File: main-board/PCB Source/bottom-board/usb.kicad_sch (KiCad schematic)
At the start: 17 parts, among them P1 USB_B, P2 USB_A, U10 TPS2001DDBVR

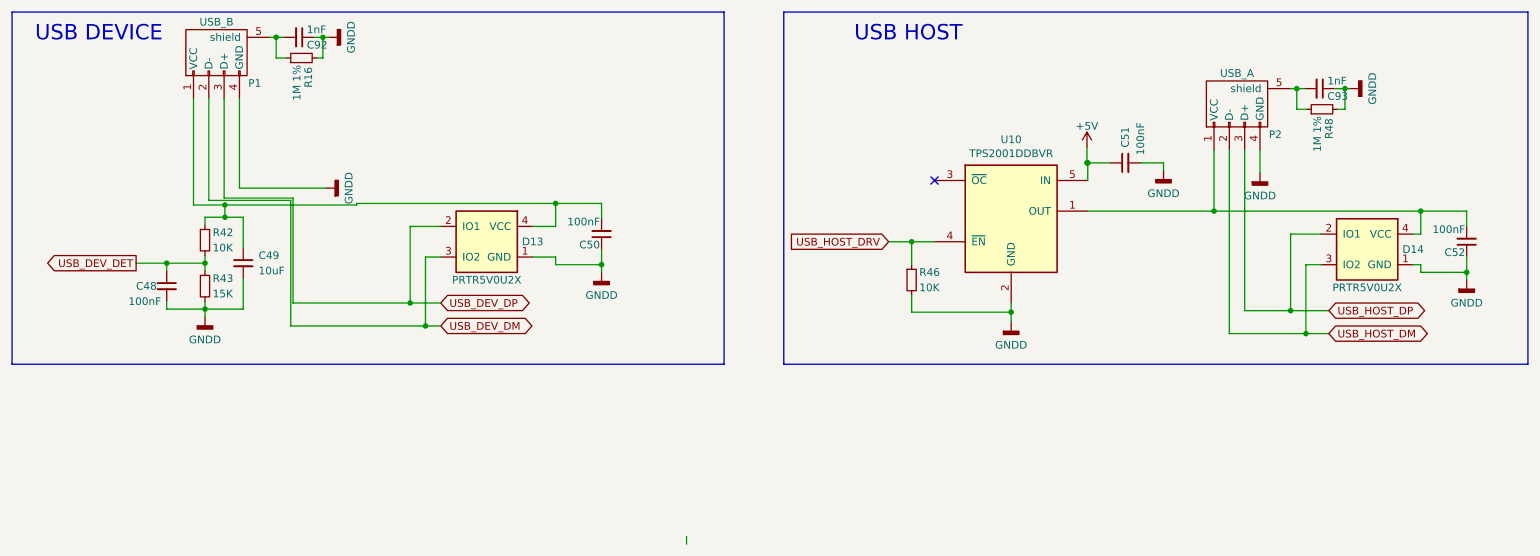
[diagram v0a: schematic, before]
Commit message: mainboard: add bias buffer, update MPNs, clean schematic
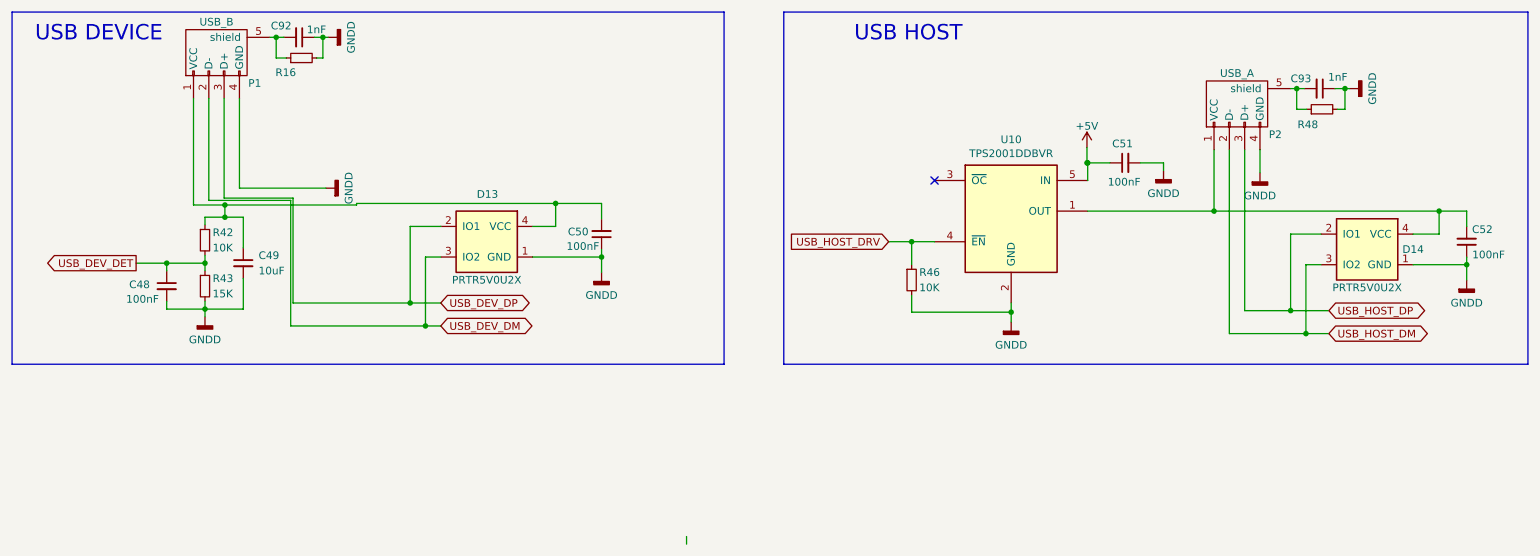
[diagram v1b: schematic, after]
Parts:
- C92, C93: MPN C0603X7R500-103KNP -> C0603X7R500-102KNP
- R16, R48: value 1M 1% -> (none); footprint Resistor_SMD:R_0603_1608Metric -> (none)

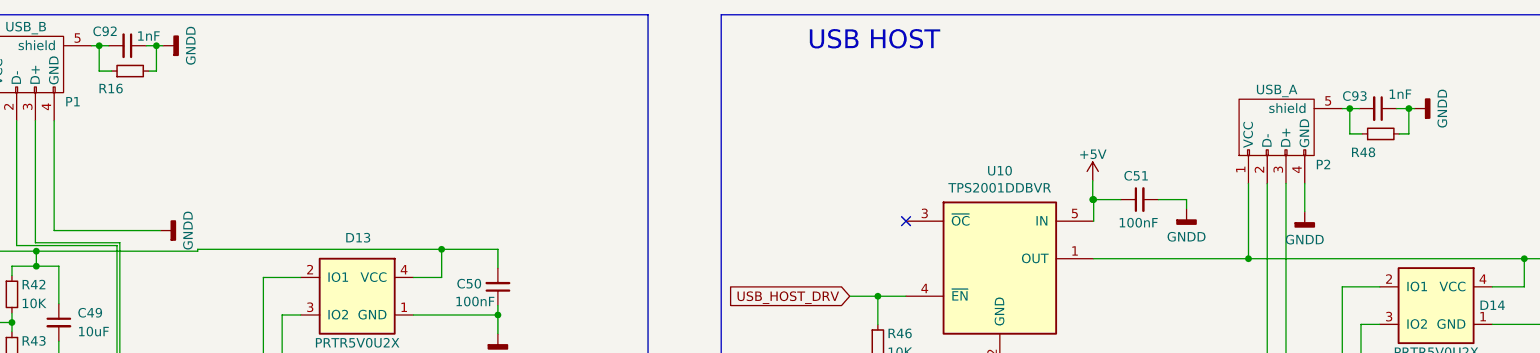
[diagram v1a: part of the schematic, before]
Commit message: mainboard: modify silkscreen
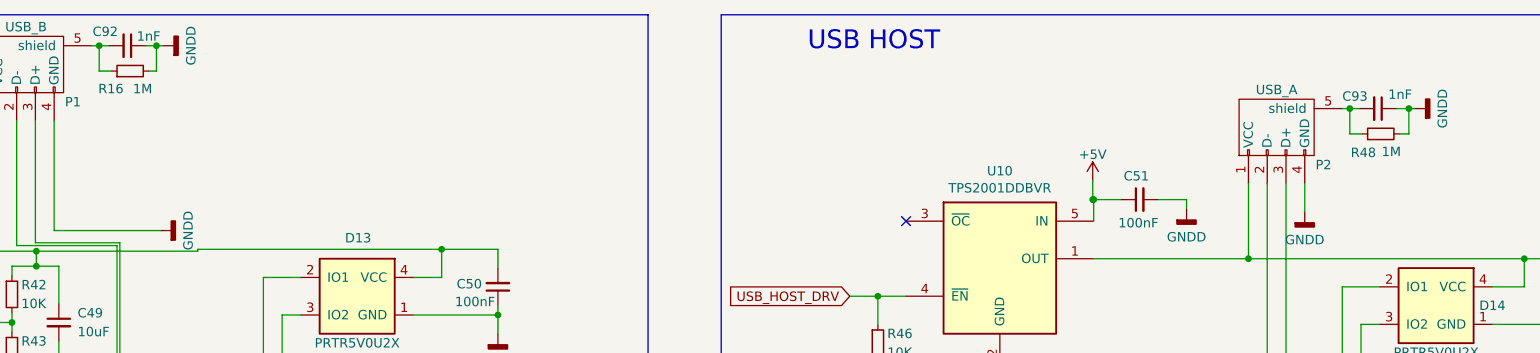
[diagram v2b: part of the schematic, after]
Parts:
- R16, R48: value (none) -> 1M; footprint (none) -> Resistor_SMD:R_0603_1608Metric
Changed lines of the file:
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@@
       (effects (font (size 1.27 1.27)) (justify right))
     )
-    (property "Value" "" (id 1) (at 71.247 64.643 90)
+    (property "Value" "1M" (id 1) (at 71.247 64.643 90)
       (effects (font (size 1.27 1.27)) (justify right))
     )
-    (property "Footprint" "" (id 2) (at 70.866 62.23 0)
+    (property "Footprint" "Resistor_SMD:R_0603_1608Metric" (id 2) (at 70.866 62.23 0)
       (effects (font (size 1.27 1.27)) hide)
     )
@@
       (effects (font (size 1.27 1.27)) (justify right))
     )
-    (property "Value" "" (id 1) (at 240.284 73.152 90)
+    (property "Value" "1M" (id 1) (at 240.284 73.152 90)
       (effects (font (size 1.27 1.27)) (justify right))
     )
-    (property "Footprint" "" (id 2) (at 240.157 70.739 0)
+    (property "Footprint" "Resistor_SMD:R_0603_1608Metric" (id 2) (at 240.157 70.739 0)
       (effects (font (size 1.27 1.27)) hide)
     )
